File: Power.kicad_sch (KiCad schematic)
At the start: 18 parts, among them J2 Barrel_Jack_Switch_Pin3Ring, U3 AP2127N-3.3, U4 AP2204RB-5.0

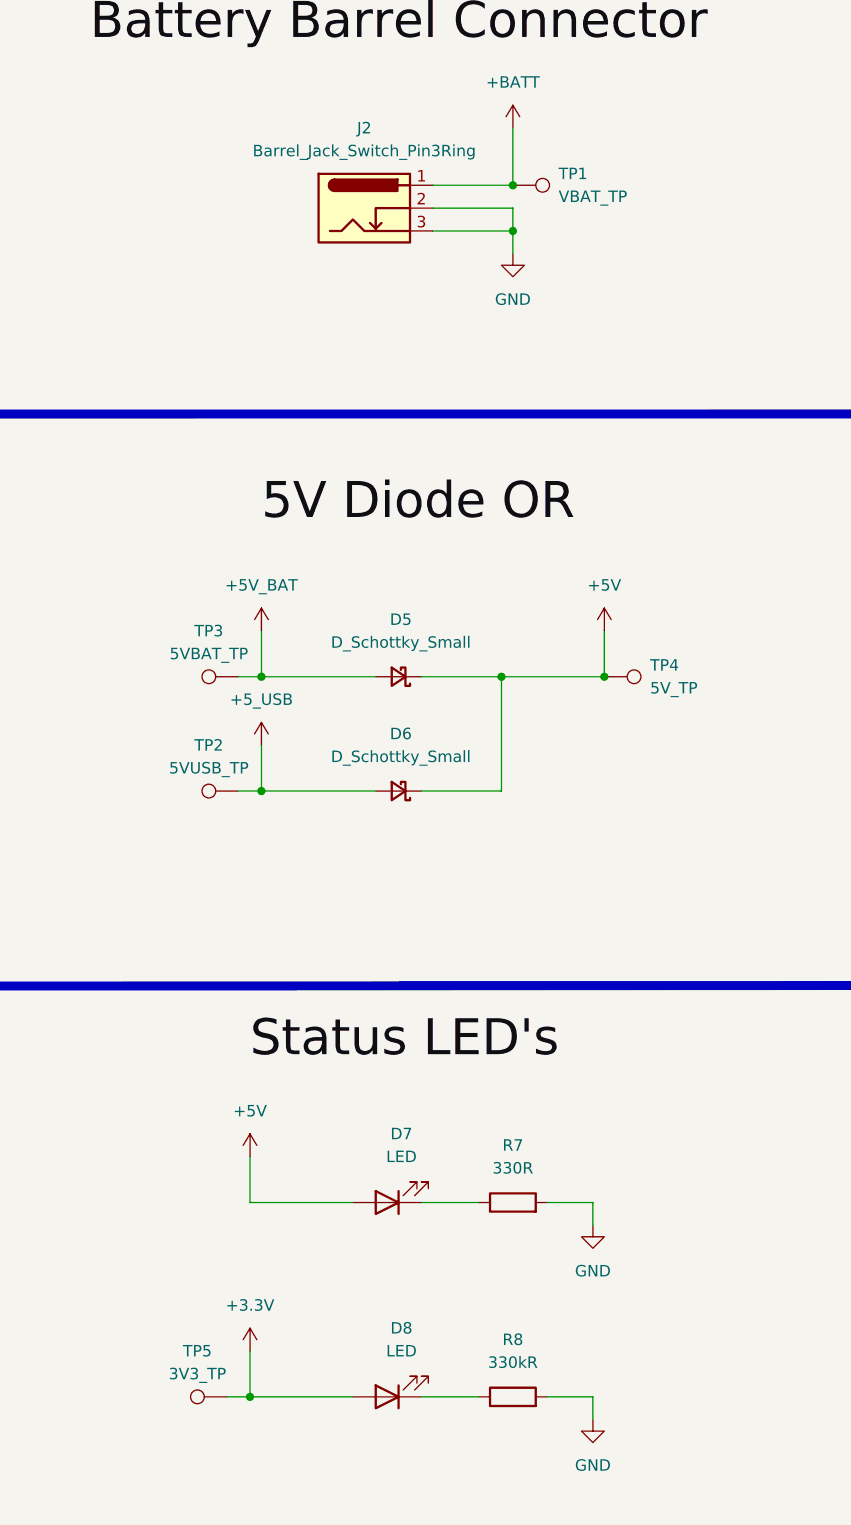
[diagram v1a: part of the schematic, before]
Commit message: Placed all components on PCB
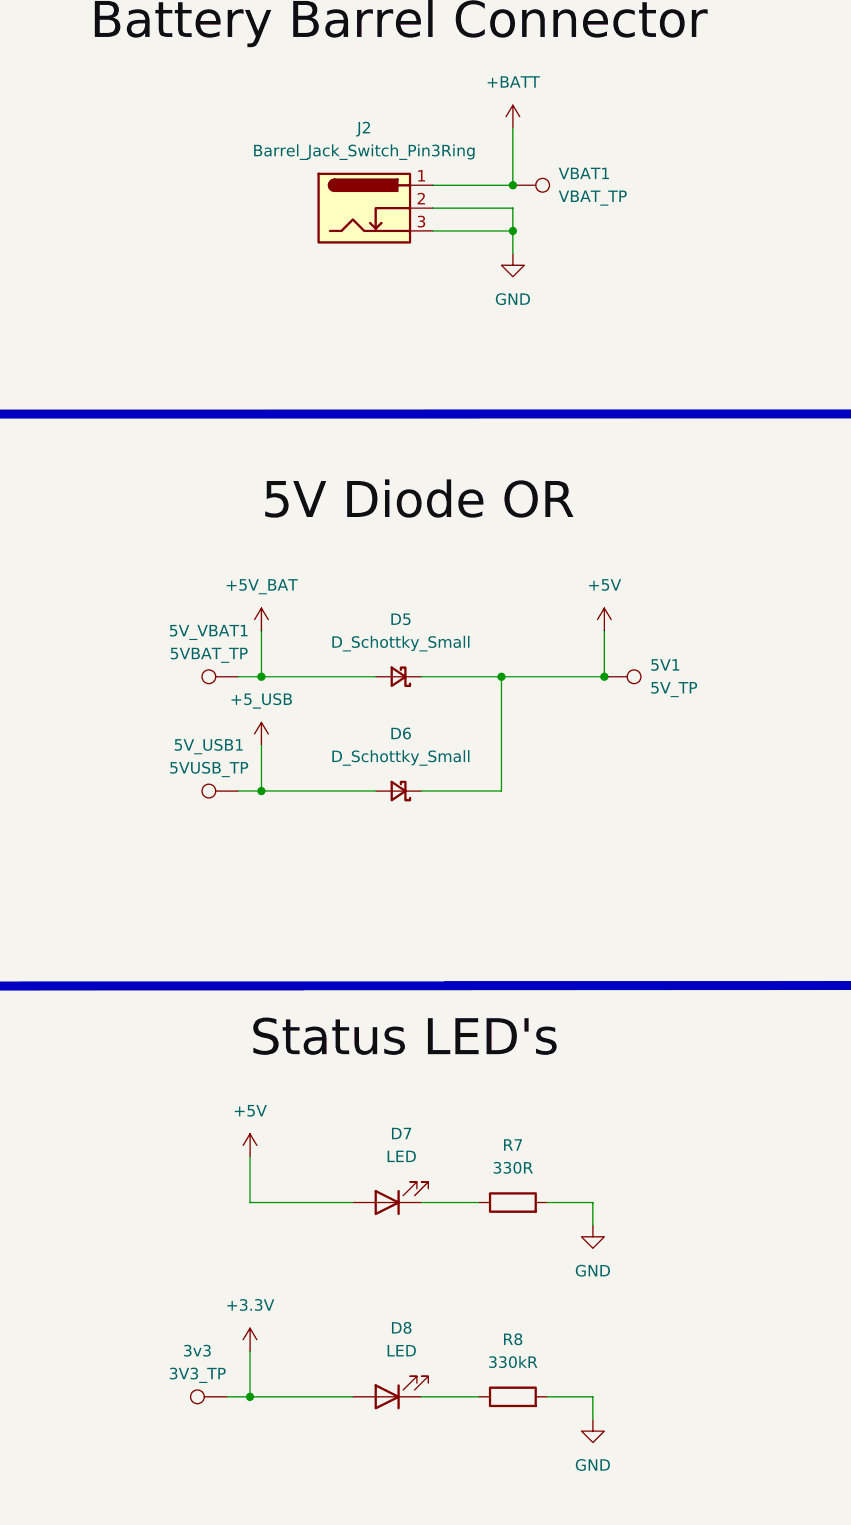
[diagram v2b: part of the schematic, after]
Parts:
- renumbered TP5 to 3v3, TP4 to 5V1, TP2 to 5V_USB1, TP3 to 5V_VBAT1, TP1 to VBAT1
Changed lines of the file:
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@@
 		(dnp no)
 		(fields_autoplaced yes)
-		(property "Reference" "TP3"
+		(property "Reference" "5V_VBAT1"
 			(at 38.608 96.52 90)
 			(effects
@@
 			(project "Airboat"
 				(path "/32966cbd-337b-4fa7-b66f-bfe62b1c18c3/bb914a23-e1b8-42c0-8b12-26fadab99985"
-					(reference "TP3")
+					(reference "5V_VBAT1")
 					(unit 1)
 				)
@@
 		(dnp no)
 		(fields_autoplaced yes)
-		(property "Reference" "TP5"
+		(property "Reference" "3v3"
 			(at 37.338 176.53 90)
 			(effects
@@
 			(project "Airboat"
 				(path "/32966cbd-337b-4fa7-b66f-bfe62b1c18c3/bb914a23-e1b8-42c0-8b12-26fadab99985"
-					(reference "TP5")
+					(reference "3v3")
 					(unit 1)
 				)
@@
 		(dnp no)
 		(fields_autoplaced yes)
-		(property "Reference" "TP1"
+		(property "Reference" "VBAT1"
 			(at 77.47 45.7199 90)
 			(effects
@@
 			(project "Airboat"
 				(path "/32966cbd-337b-4fa7-b66f-bfe62b1c18c3/bb914a23-e1b8-42c0-8b12-26fadab99985"
-					(reference "TP1")
+					(reference "VBAT1")
 					(unit 1)
 				)
@@
 		(dnp no)
 		(fields_autoplaced yes)
-		(property "Reference" "TP4"
+		(property "Reference" "5V1"
 			(at 87.63 100.3299 90)
 			(effects
@@
 			(project "Airboat"
 				(path "/32966cbd-337b-4fa7-b66f-bfe62b1c18c3/bb914a23-e1b8-42c0-8b12-26fadab99985"
-					(reference "TP4")
+					(reference "5V1")
 					(unit 1)
 				)
@@
 		(dnp no)
 		(fields_autoplaced yes)
-		(property "Reference" "TP2"
+		(property "Reference" "5V_USB1"
 			(at 38.608 109.22 90)
 			(effects
@@
 			(project "Airboat"
 				(path "/32966cbd-337b-4fa7-b66f-bfe62b1c18c3/bb914a23-e1b8-42c0-8b12-26fadab99985"
-					(reference "TP2")
-					(unit 1)
-				)
+					(reference "5V_USB1")
+					(unit 1)
+				)

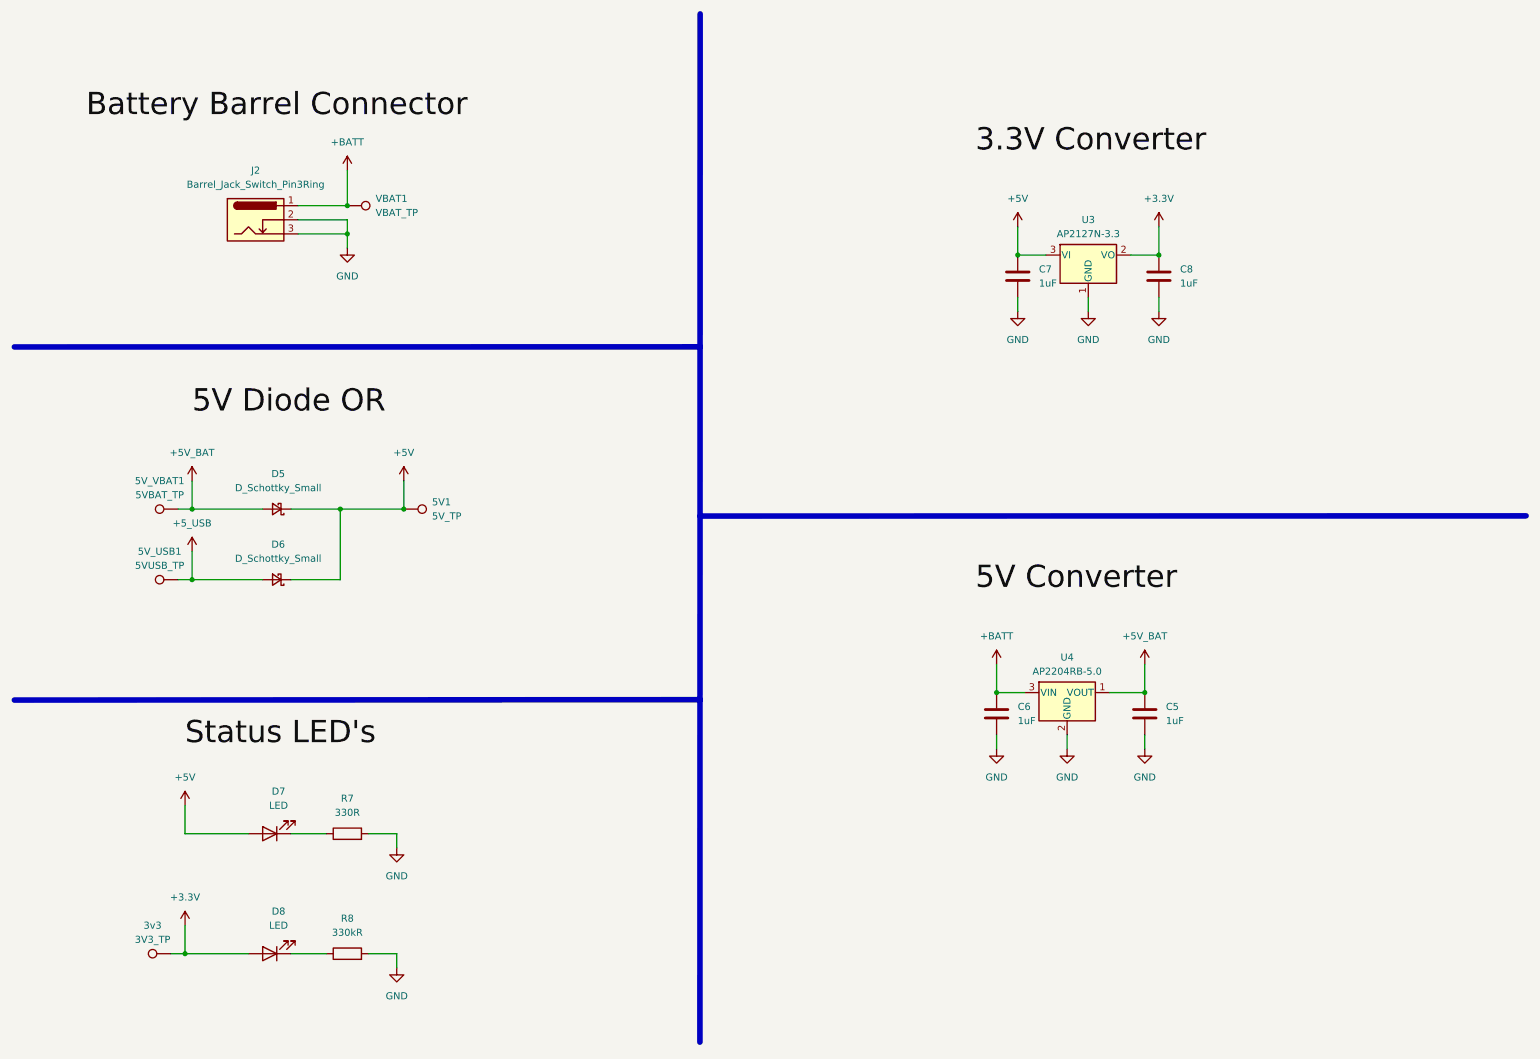
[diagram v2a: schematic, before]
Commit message: Removed uneeeded components, started to lay PCB traces
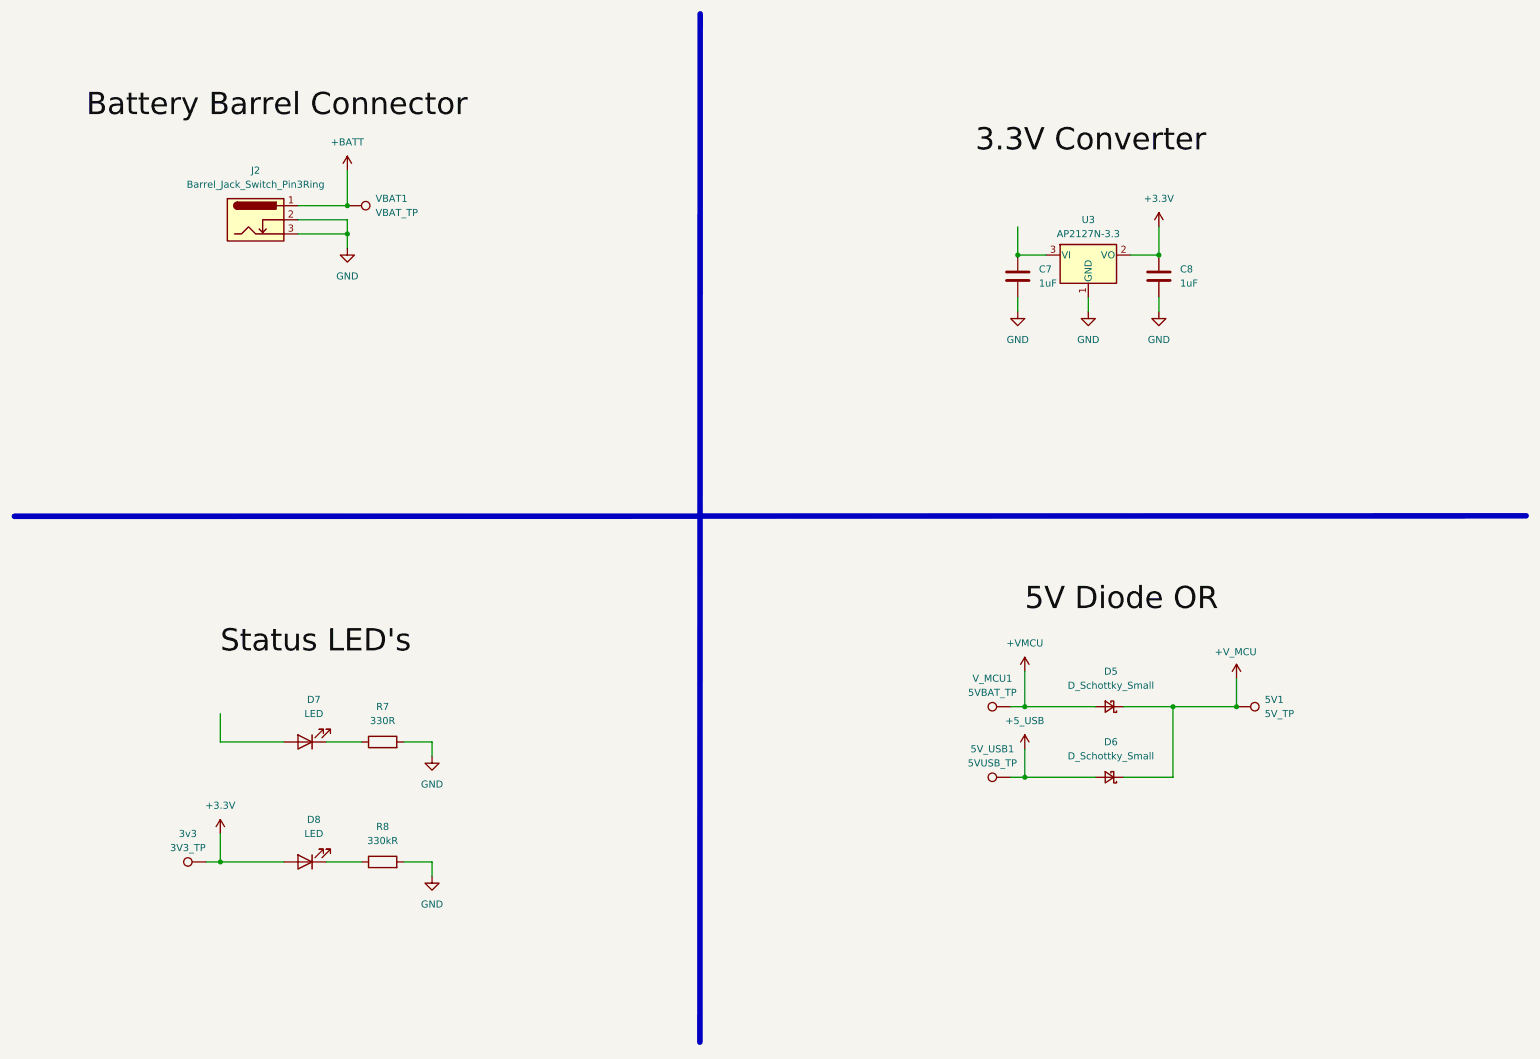
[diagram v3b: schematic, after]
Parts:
- removed 5V_VBAT1: 5VBAT_TP, TestPoint:TestPoint_Pad_D2.0mm, symbol Connector:TestPoint
- removed C5, C6: 1uF, Capacitor_SMD:C_0603_1608Metric_Pad1.08x0.95mm_HandSolder, symbol Device:C
- removed U4: AP2204RB-5.0, Package_TO_SOT_SMD:SOT-89-3, symbol Regulator_Linear:AP2204RB-5.0
- added V_MCU1: 5VBAT_TP, TestPoint:TestPoint_Pad_D2.0mm, symbol Connector:TestPoint
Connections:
- net +5V renamed +V_MCU
- net +V_MCU: no longer C7.1, D7.2 (A), U3.3 (VI)
- net +5V_BAT renamed +VMCU
- net +VMCU: now also V_MCU1.1
- new net: C7.1, U3.3 (VI)
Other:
- moved on the sheet: 3v3, D7, D8, R7, R8
